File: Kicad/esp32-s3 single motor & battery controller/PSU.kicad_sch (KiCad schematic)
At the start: 22 parts, among them Q3 PMOS,Si7157DP, Q4 PMOS, U1 AP2112K-3.3, U4 BQ25060

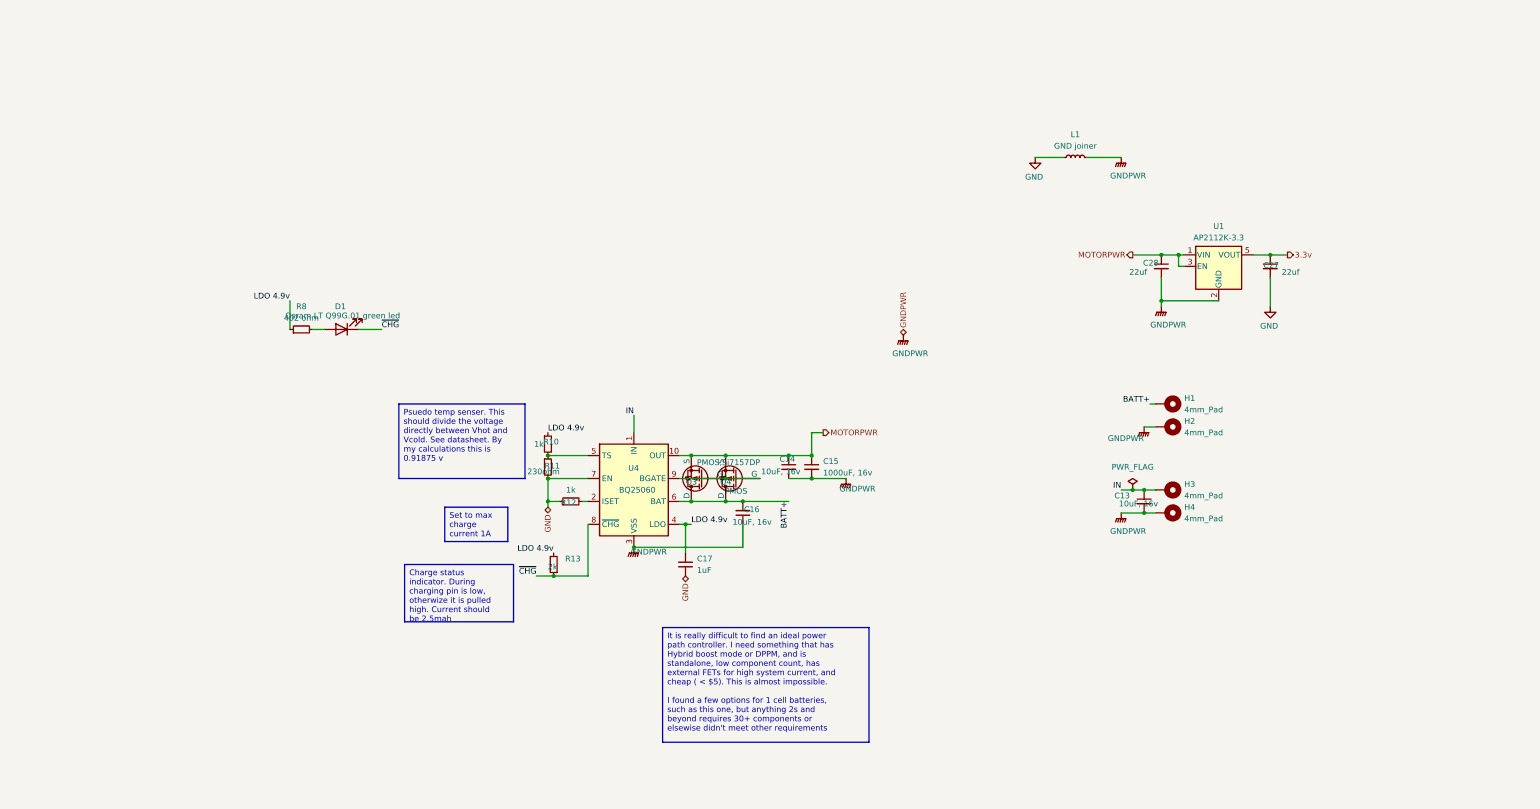
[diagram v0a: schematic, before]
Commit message: Starting work on replacing battery charger with 2s version
The charger module will be way too big, but I really think I need this. Hopefully I can find a more integrated charger
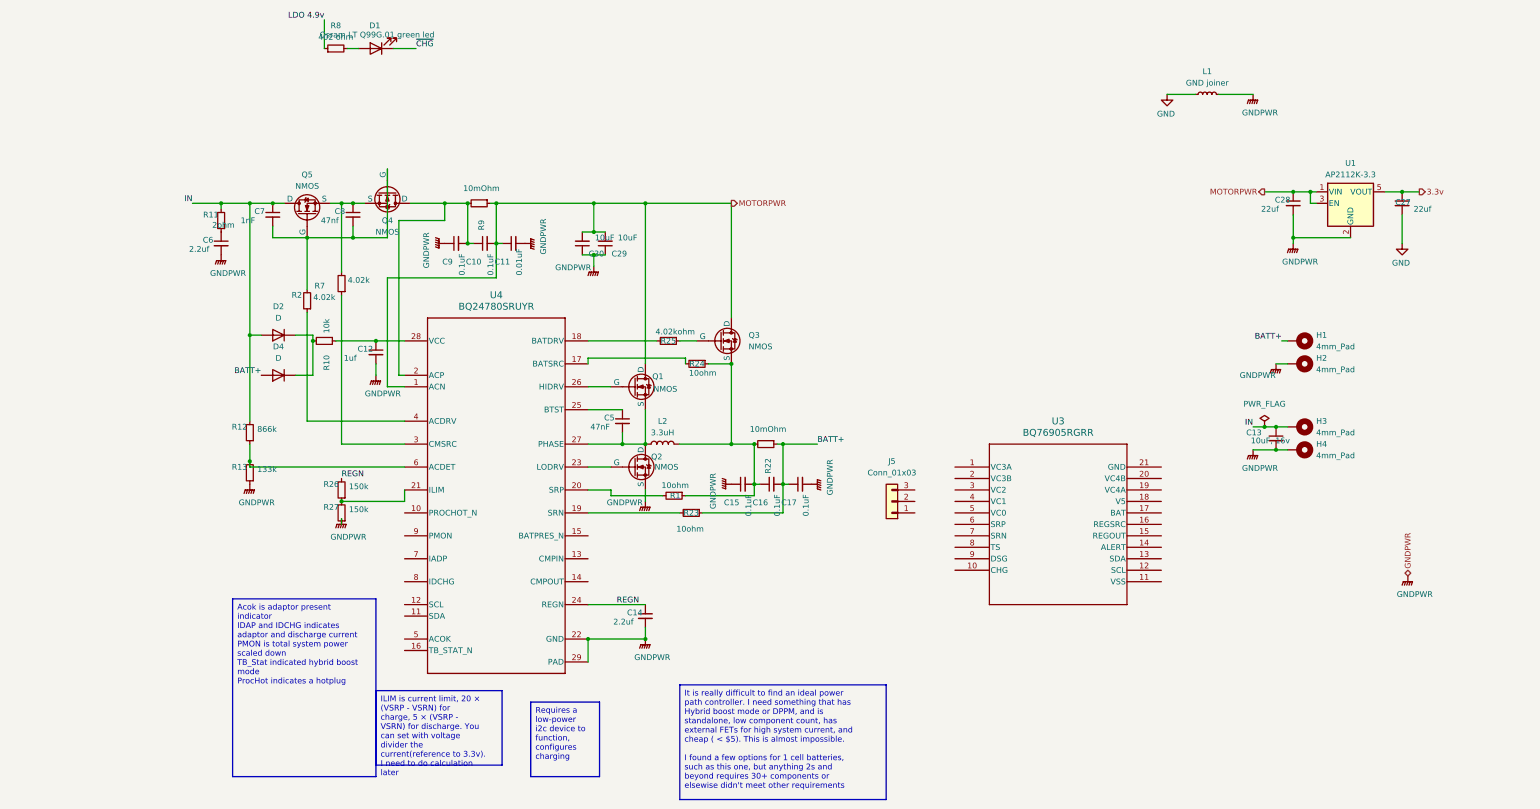
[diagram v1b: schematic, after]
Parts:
- removed Q3: PMOS,Si7157DP, Package_DFN_QFN:PQFN-8-EP_6x5mm_P1.27mm_Generic, symbol Simulation_SPICE:PMOS
- removed Q4: PMOS, Package_DFN_QFN:PQFN-8-EP_6x5mm_P1.27mm_Generic, symbol Simulation_SPICE:PMOS
- removed U4: BQ25060, custom_Power:WSON-10-1EP_2x3mm_P0.5mm_EP0.84x2.4mm_ThermalVias_0.3mm, symbol custom_Battery_Management:BQ25060
- added C10, C9: 0.1uF, Capacitor_SMD:C_0603_1608Metric, symbol Device:C_Small
- added C11: 0.01uF, Capacitor_SMD:C_0603_1608Metric, symbol Device:C_Small
- added C12: 1uf, Capacitor_SMD:C_0603_1608Metric, symbol Device:C_Small
- added C29, C30: 10uF, Capacitor_SMD:C_0603_1608Metric, symbol Device:C_Small
- added C5: 47nF, Capacitor_SMD:C_0603_1608Metric, symbol Device:C_Small
- added C6: 2.2uf, Capacitor_SMD:C_0603_1608Metric, symbol Device:C_Small
- added C7: 1nF, Capacitor_SMD:C_0603_1608Metric, symbol Device:C_Small
- added C8: 47nf, Capacitor_SMD:C_0603_1608Metric, symbol Device:C_Small
- added D2, D4: D, symbol Device:D
- added J5: Conn_01x03, symbol Connector_Generic:Conn_01x03
- added L2: 3.3uH, symbol Device:L
- added Q1, Q2, Q3, Q4, Q5: NMOS, symbol Simulation_SPICE:NMOS
- added R1, R23, R24: 10ohm, Resistor_SMD:R_0603_1608Metric, symbol Device:R_Small
- added R2, R7: 4.02k, Resistor_SMD:R_0603_1608Metric, symbol Device:R_Small
- added R22, R9: 10mOhm, Resistor_SMD:R_0603_1608Metric, symbol Device:R_Small
- added R25: 4.02kohm, Resistor_SMD:R_0603_1608Metric, symbol Device:R_Small
- added R26, R27: 150k, Resistor_SMD:R_0603_1608Metric, symbol Device:R_Small
- added U3: BQ76905RGRR, VQFN20_RGR_TEX, symbol BQ76905:BQ76905RGRR
- added U4: BQ24780SRUYR, RUY0028A, symbol BQ24780s:BQ24780SRUYR
- C14: value 10uF, 16v -> 2.2uf; footprint Capacitor_SMD:C_0603_1608Metric_Pad1.08x0.95mm_HandSolder -> Capacitor_SMD:C_0603_1608Metric
- C15: value 1000uF, 16v -> 0.1uF; footprint Capacitor_THT:C_Radial_D5.0mm_H5.0mm_P2.00mm -> Capacitor_SMD:C_0603_1608Metric
- C16: value 10uF, 16v -> 0.1uF; footprint Capacitor_SMD:C_0603_1608Metric_Pad1.08x0.95mm_HandSolder -> Capacitor_SMD:C_0603_1608Metric
- C17: value 1uF -> 0.1uF; footprint Capacitor_SMD:C_0603_1608Metric_Pad1.08x0.95mm_HandSolder -> Capacitor_SMD:C_0603_1608Metric
- R10: value 1k -> 10k; footprint Resistor_SMD:R_0603_1608Metric_Pad0.98x0.95mm_HandSolder -> Resistor_SMD:R_0603_1608Metric
- R11: value 230ohm -> 2ohm; footprint Resistor_SMD:R_0603_1608Metric_Pad0.98x0.95mm_HandSolder -> Resistor_SMD:R_0603_1608Metric
- R12: value 1k -> 866k; footprint Resistor_SMD:R_0603_1608Metric_Pad0.98x0.95mm_HandSolder -> Resistor_SMD:R_0603_1608Metric
- R13: value 2k -> 133k; footprint Resistor_SMD:R_0603_1608Metric_Pad0.98x0.95mm_HandSolder -> Resistor_SMD:R_0603_1608Metric
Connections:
- net BATT+: now also C17.1, D4.2 (A), R22.1, R23.1
- net GND: no longer C17.1, R11.2, R12.1
- net GNDPWR: now also C15.1, C17.2, R13.1, C11.2, C12.2, C29.1, C30.1, C6.2, C9.1, Q2.3 (S), R27.1, U4.22 (GND), U4.29 (PAD); no longer C15.2, C16.1
- net IN: now also R11.2, R12.2, C7.1, D2.2 (A), Q5.1 (D)
- net LDO 4.9v: no longer C17.2, R10.1, R13.2
- net MOTORPWR: now also C10.2, C11.1, C29.2, C30.2, Q1.1 (D), Q3.1 (D), R9.1, U4.1 (ACN); no longer C14.1, C15.1
- net ~{CHG}: no longer R13.1
- net at R10.2: now also D2.1 (K), D4.1 (K); no longer R11.1
- new net: R23.2, U4.19 (SRN)
- new net: R26.1, R27.2, U4.21 (ILIM)
- new net: C12.1, R10.1, U4.28 (VCC)
- new net: C10.1, C9.2, Q4.1 (D), R9.2, U4.2 (ACP)
- new net: C7.2, C8.2, Q4.2 (G), Q5.2 (G), R2.2
- new net: C8.1, Q4.3 (S), Q5.3 (S), R7.2
- new net: C5.1, U4.25 (BTST)
- new net: C5.2, L2.1, Q1.3 (S), Q2.1 (D), U4.27 (PHASE)
- new net: C15.2, C16.1, L2.2, Q3.3 (S), R1.1, R22.2, R24.1
- new net: R24.2, U4.17 (BATSRC)
- new net: R7.1, U4.3 (CMSRC)
- new net: R2.1, U4.4 (ACDRV)
- new net: Q3.2 (G), R25.1
- new net: R25.2, U4.18 (BATDRV)
- new net: C6.1, R11.1
- new net: R1.2, U4.20 (SRP)
- new net: Q2.2 (G), U4.23 (LODRV)
- new net: Q1.2 (G), U4.26 (HIDRV)
- new net: R12.1, R13.2, U4.6 (ACDET)
- new net REGN: C14.1, R26.2, U4.24 (REGN)
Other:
- moved on the sheet: C13, C27, C28, D1, H1, H2, H3, H4, L1, R8, U1

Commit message: Finished charger, added balancer circuitry
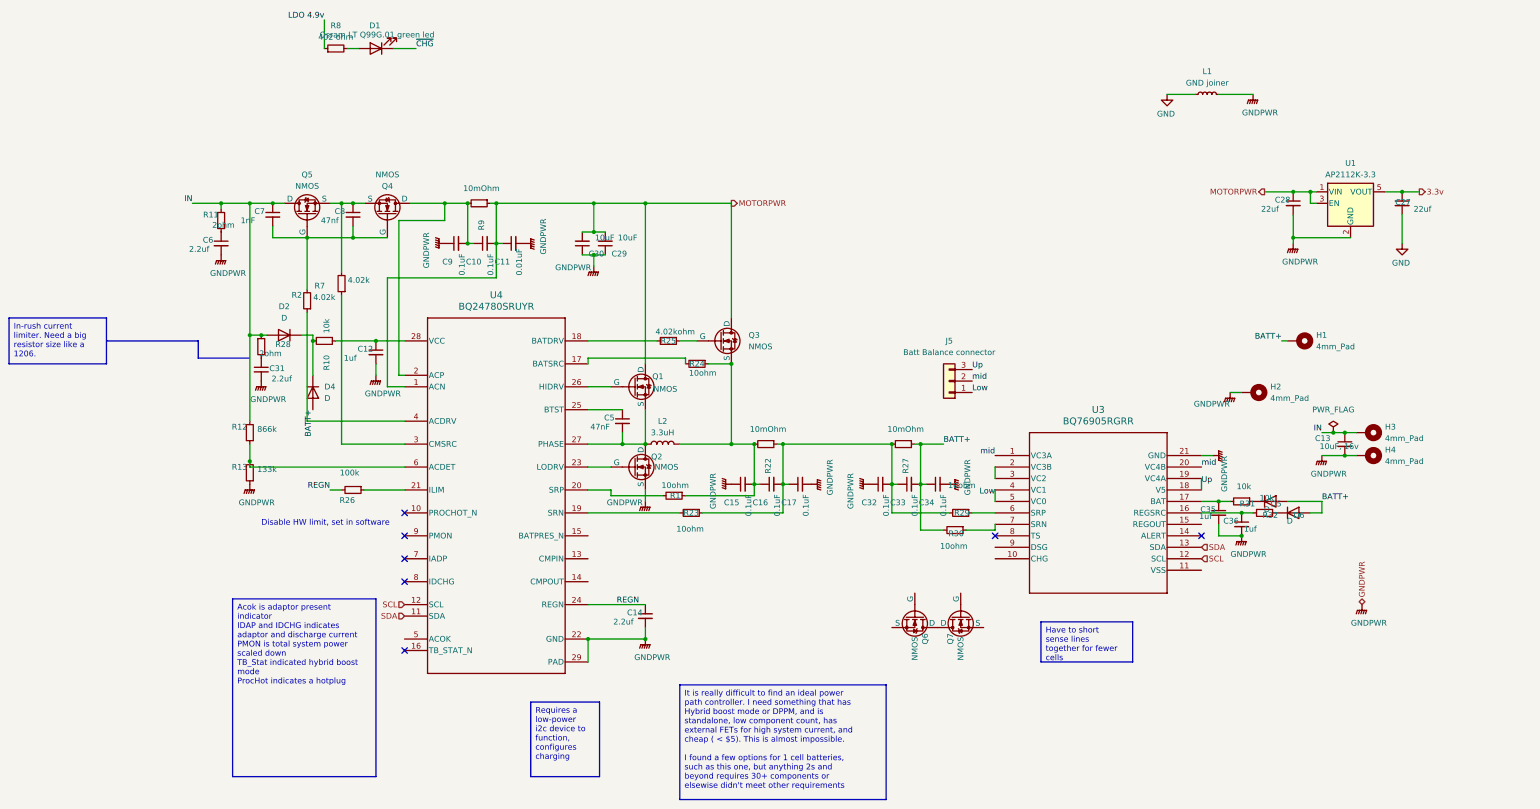
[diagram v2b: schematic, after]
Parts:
- added C31: 2.2uf, Capacitor_SMD:C_0603_1608Metric, symbol Device:C_Small
- added C32, C33, C34: 0.1uF, Capacitor_SMD:C_0603_1608Metric, symbol Device:C_Small
- added C35, C36: 1uf, Capacitor_SMD:C_0603_1608Metric, symbol Device:C_Small
- added D5, D6: D, symbol Device:D
- added Q6, Q7: NMOS, symbol Simulation_SPICE:NMOS
- added R28: 2ohm, Resistor_SMD:R_0603_1608Metric, symbol Device:R_Small
- added R29, R30: 10ohm, Resistor_SMD:R_0603_1608Metric, symbol Device:R_Small
- added R31, R32: 10k, Resistor_SMD:R_0603_1608Metric, symbol Device:R_Small
- J5: value Conn_01x03 -> Batt Balance connector
- R26: value 150k -> 100k
- R27: value 150k -> 10mOhm
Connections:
- net BATT+: now also R27.1, C33.2, C34.1, D5.2 (A), D6.2 (A), R30.2; no longer C16.2, C17.1, R22.1, R23.1
- net GNDPWR: now also U3.21 (GND), C31.2, C32.1, C34.2, C35.2, C36.2; no longer R27.1
- net IN: now also R28.1
- net at R26.1, U4.21 (ILIM): no longer R27.2
- net Low: now reaches J5.1 (Pin_1)
- net Low: now also U3.4 (VC1), U3.5 (VC0)
- net mid: now reaches J5.2 (Pin_2)
- net mid: now also U3.1 (VC3A), U3.20 (VC4B)
- net Up: now reaches J5.3 (Pin_3)
- net Up: now also U3.18 (V5), U3.19 (VC4A)
- net SDA: now reaches U4.11 (SDA)
- net SDA: now also U3.13 (SDA)
- net SCL: now reaches U4.12 (SCL)
- net SCL: now also U3.12 (SCL)
- net at U3.16 (REGSRC): now also C36.1, R32.2
- net at U3.17 (BAT): now also C35.1, R31.2
- net at U3.2 (VC3B): now also U3.3 (VC2)
- net at U3.6 (SRP): now also R29.1
- net at U3.7 (SRN): now also R30.1
- new net: C16.2, C17.1, C32.2, C33.1, R22.1, R23.1, R27.2, R29.2
- new net: D5.1 (K), R31.1
- new net: C31.1, R28.2
- new net: D6.1 (K), R32.1
- new net: Q6.1 (D), Q7.1 (D)
- no-connect marks 0 -> 7
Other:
- note added: "Disable HW limit, set in software"
- moved on the sheet: C13, D2, D4, H2, H3, H4, J5, Q4, U3

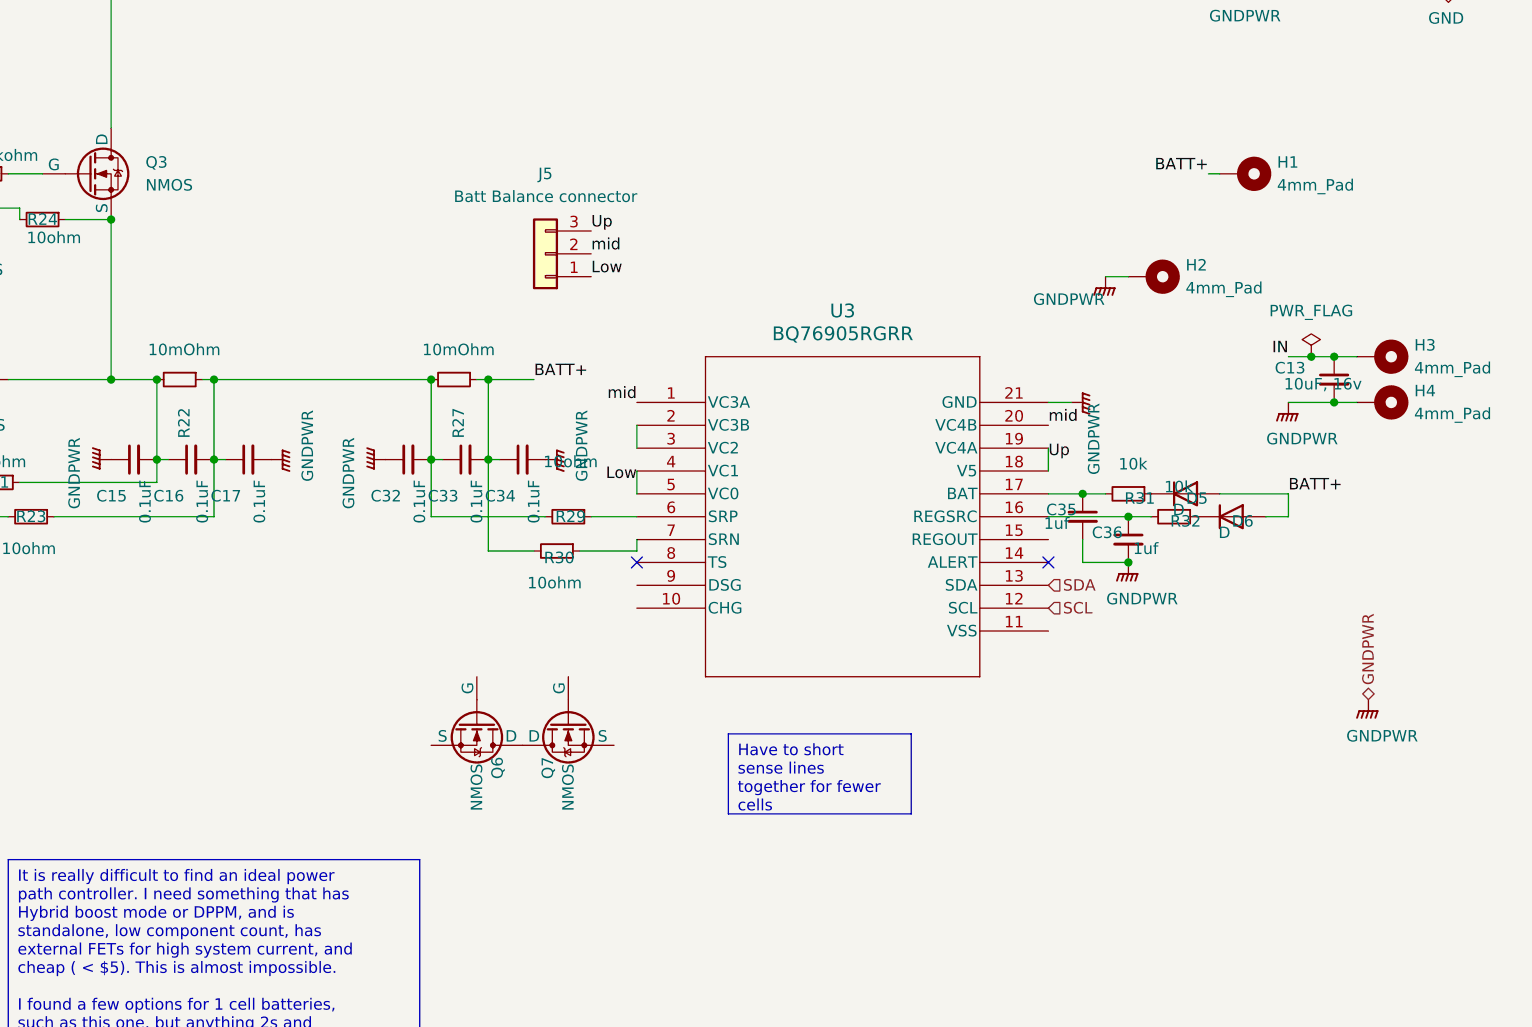
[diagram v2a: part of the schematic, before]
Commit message: Finished basic balance charge circuit
Passive values still need to be tweaked, and the datasheet needs to be checked again.
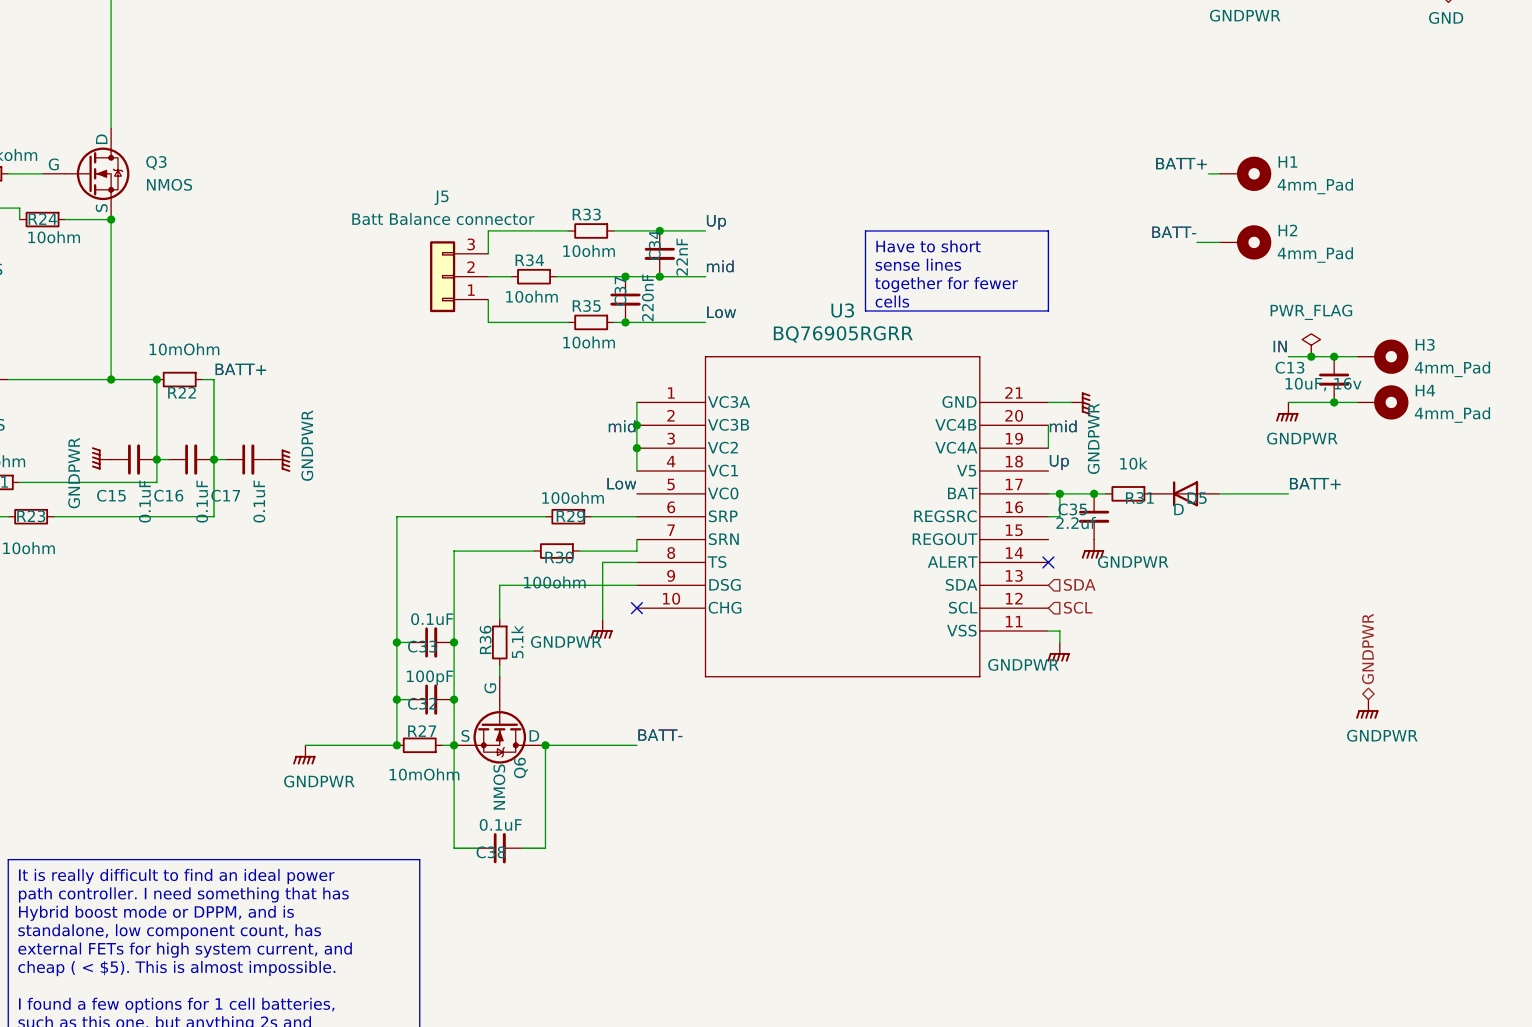
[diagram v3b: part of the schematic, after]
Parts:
- removed C36: 1uf, Capacitor_SMD:C_0603_1608Metric, symbol Device:C_Small
- removed D6: D, symbol Device:D
- removed Q7: NMOS, symbol Simulation_SPICE:NMOS
- removed R32: 10k, Resistor_SMD:R_0603_1608Metric, symbol Device:R_Small
- added C37: 220nF, Capacitor_SMD:C_0603_1608Metric, symbol Device:C_Small
- added C38: 0.1uF, Capacitor_SMD:C_0603_1608Metric, symbol Device:C_Small
- added R33, R34, R35: 10ohm, Resistor_SMD:R_0603_1608Metric, symbol Device:R_Small
- added R36: 5.1k, Resistor_SMD:R_0603_1608Metric, symbol Device:R_Small
- C32: value 0.1uF -> 100pF
- C34: value 0.1uF -> 22nF
- C35: value 1uf -> 2.2uf
- R29, R30: value 10ohm -> 100ohm
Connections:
- net BATT+: now also C16.2, C17.1, R22.1, R23.1; no longer C33.2, C34.1, R27.1, R30.2
- net GNDPWR: now also C33.1, R27.2, R29.2, U3.11 (VSS), U3.8 (TS); no longer C34.2, H2.1
- net Low: now also C37.2, R35.1; no longer J5.1 (Pin_1), U3.4 (VC1)
- net Up: now also C34.1, R33.1; no longer J5.3 (Pin_3), U3.19 (VC4A)
- net mid: now also C34.2, U3.19 (VC4A), U3.2 (VC3B), U3.3 (VC2), U3.4 (VC1), C37.1, R34.1; no longer J5.2 (Pin_2)
- net at U3.16 (REGSRC): now also C35.1, R31.2, U3.17 (BAT)
- net BATT-: now reaches Q6.1 (D)
- net BATT-: now also H2.1, C38.2
- net at U3.9 (DSG): now also R36.1
- net at Q6.2 (G): now also R36.2
- net at Q6.3 (S): now also C32.2, C33.2, R27.1, R30.2, C38.1
- new net: J5.1 (Pin_1), R35.2
- new net: J5.2 (Pin_2), R34.2
- new net: J5.3 (Pin_3), R33.2
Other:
- moved on the sheet: C33, C35, H2, J5, Q6, R27
